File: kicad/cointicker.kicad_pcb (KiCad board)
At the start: 2 copper layers, 45 x 30 mm, 25 parts, among them J1 USB_B_Micro, Q1 PUMX1, Q2 S8050_J3Y, U1 ESP-12E, U2 CP2102-GMR_NRND, U3 BL8565

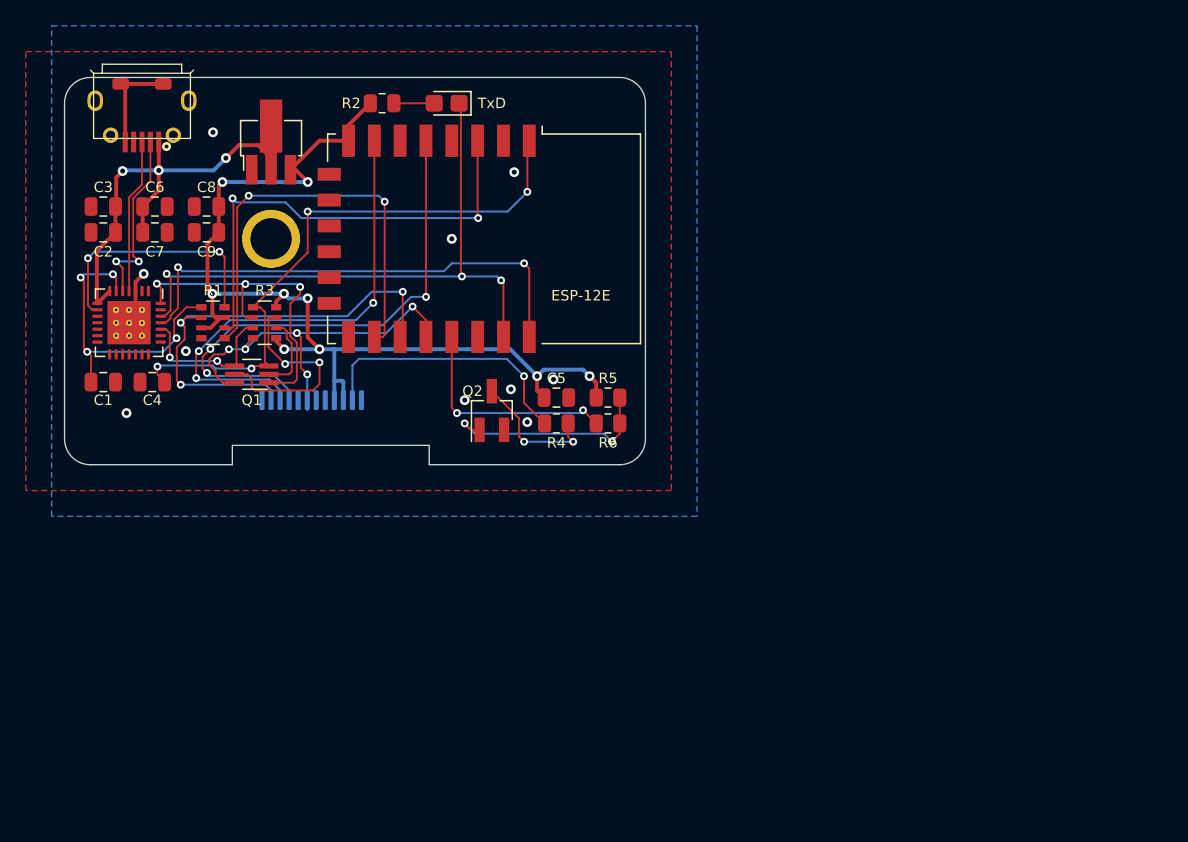
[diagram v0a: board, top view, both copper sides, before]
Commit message: used updated display footprint...
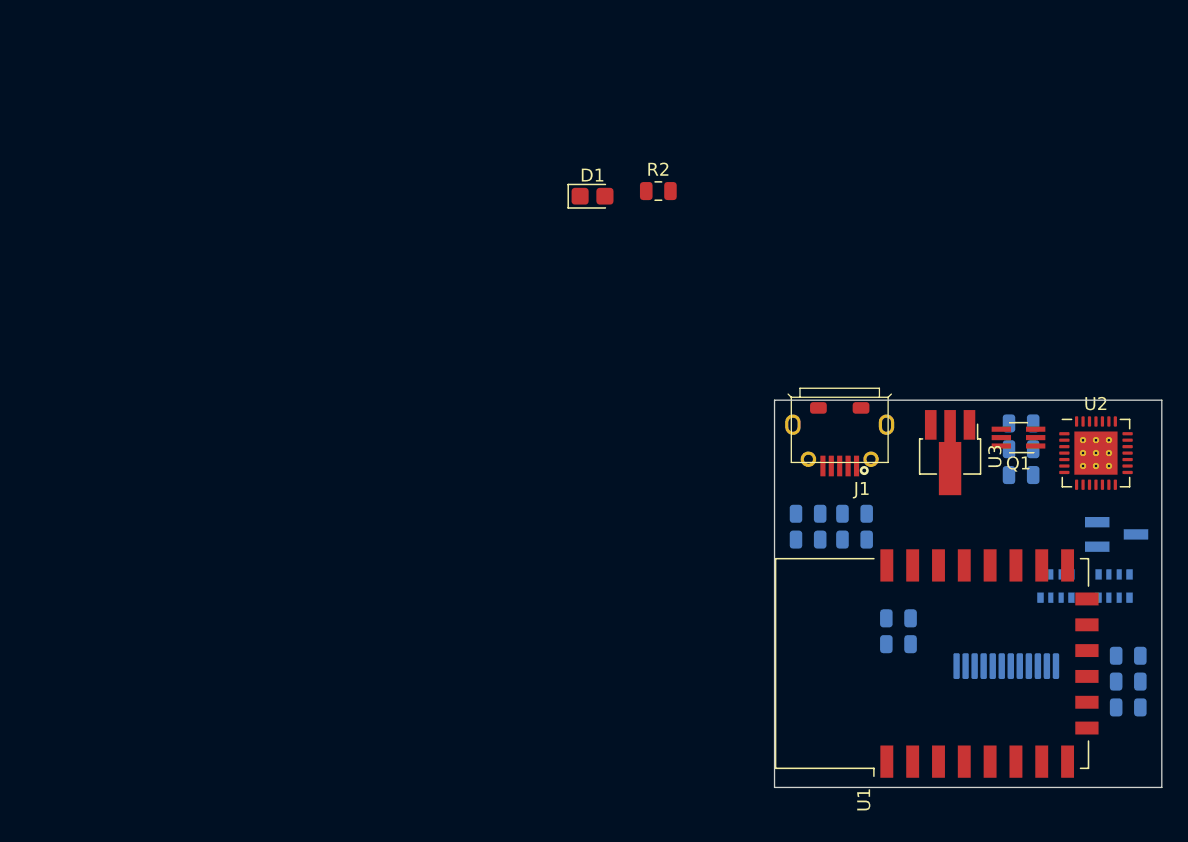
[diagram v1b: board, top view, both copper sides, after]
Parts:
- removed QR*****: https://github.com/gerdmuller/Coin-Ticker, https:__github.com_gerdmuller_Coin-Ticker
- removed REF**: PTH Hole, PTH_Hole
- C1, C2, C3, C4, C5, C6, C7, C8, C9, Q2, R1, R3, R4, R5, R6: moved to B.Cu
- D2: footprint barn53-kicad:IPSDisplay_240x240_FPC_15 -> barn53-kicad:IPSDisplay_240x240_FPC_80deg
- moved U2 75.6 mm to (129.9, 59.1), turned to 0 degrees
- moved C3 74.1 mm to (124.1, 60.8), turned to 0 degrees
- moved C2 73.1 mm to (124.1, 58.8), turned to 0 degrees
- moved C1 71.2 mm to (124.1, 56.8), turned to 180 degrees
- moved R3 68.9 mm to (131.3, 69.4), turned to 270 degrees
- moved R1 68.4 mm to (126.8, 69.4), turned to 270 degrees
- moved C4 60.6 mm to (114.6, 71.9), turned to 0 degrees
- moved Q1 59.6 mm to (123.9, 57.9)
- moved J1 59.6 mm to (110.0, 60.1)
- moved U3 57.8 mm to (118.6, 59.1), turned to 270 degrees
- moved C6 56.8 mm to (107.6, 65.8)
- moved C8 55.6 mm to (111.2, 63.8)
- moved C9 55.6 mm to (111.2, 65.8)
- moved C7 55.1 mm to (107.6, 63.8)
- moved D2 51.3 mm to (120.0, 75.6)
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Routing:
- net +3V3: track 80.6 -> 0.00 mm, vias 9 -> 0
- net TxD: track 48.0 -> 0.00 mm, vias 3 -> 0
- net /~Reset: track 46.5 -> 0.00 mm, vias 4 -> 0
- net /TFT_SCL: track 40.4 -> 0.00 mm, vias 3 -> 0
- net /RxD: track 38.1 -> 0.00 mm, vias 2 -> 0
- net /TFT_SDA: track 37.5 -> 0.00 mm, vias 3 -> 0
- net /~TFT_RES: track 36.8 -> 0.00 mm, vias 3 -> 0
- net Net-(R1-Pad6): track 36.3 -> 0.00 mm, vias 2 -> 0
- net Net-(R1-Pad5): track 33.8 -> 0.00 mm, vias 2 -> 0
- net VBUS: track 33.7 -> 0.00 mm, vias 3 -> 0
- net /GPIO0: track 30.8 -> 0.00 mm, vias 5 -> 0
- net /DTR: track 26.2 -> 0.00 mm, vias 3 -> 0
- net /VDD: track 23.8 -> 0.00 mm, vias 4 -> 0
- net /LEDK: track 21.1 -> 0.00 mm, vias 1 -> 0
- net Net-(R1-Pad8): track 19.4 -> 0.00 mm, vias 2 -> 0
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- removed copper zone on B.Cu, net GND
- removed copper zone on F.Cu, net GND
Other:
- board size 45 x 30 mm -> 30 x 30 mm
- copper layers 2 -> 4
- net class Default: via_dia 0.6096 -> 0.6; via_drill 0.3048 -> 0.3
- net class Minimal added: clearance 0.127, trace_width 0.127, via_dia 0.45, via_drill 0.2
- net class Power: clearance 0.127 -> 0.254; via_dia 0.762 -> 0.6; via_drill 0.381 -> 0.3
- rule via_min_drill: 0.3048 -> 0.2
- rule via_min_size: 0.6096 -> 0.45
- board text removed: "To The Moon!"
- board text removed: "barn53 CoinTicker rev.A 01/21 IPS Display 240x240 16Bit Color"
